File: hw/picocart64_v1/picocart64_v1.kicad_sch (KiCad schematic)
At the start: 16 parts, among them J1 USB_C_Receptacle_USB2.0, J2 Conn_01x05, J3 Conn_02x06_Odd_Even, J4 Micro_SD_Card_Det, Q1 BSS84, SW1 BootButton, U3 RP2040_Stamp, U4 N64-Cartridge

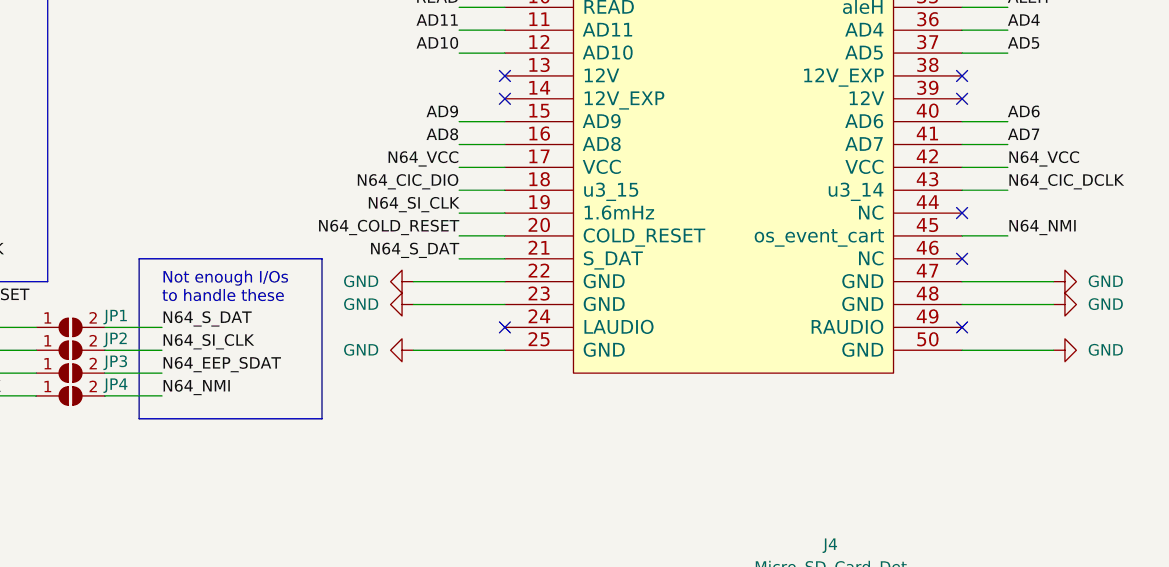
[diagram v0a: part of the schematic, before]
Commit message: hw: PicoCart64 V1.1
- KiCad project files
- Gerbers
- PDF
- Changelog since V1.0 + errata
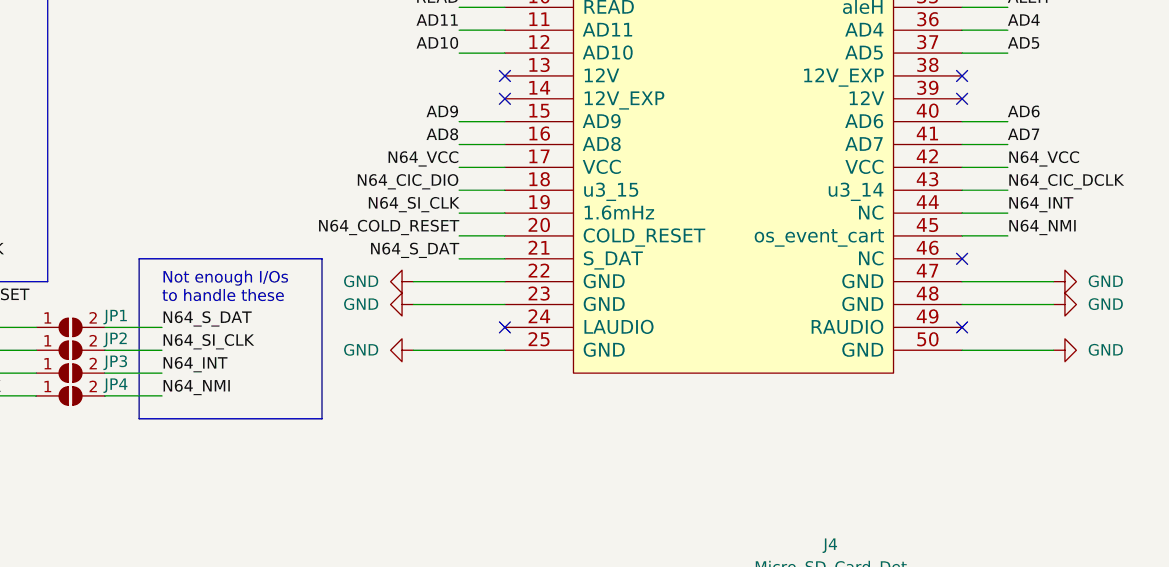
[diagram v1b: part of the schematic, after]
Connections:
- net N64_EEP_SDAT is gone; now on net N64_INT: JP3.2 (B)
- net N64_INT: now reaches U4.44 (NC)
- no-connect marks 12 -> 11
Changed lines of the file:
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@@
   (title_block
     (title "PicoCart64")
-    (date "2022-06-22")
-    (rev "V1.0")
+    (date "2022-07-02")
+    (rev "V1.1")
     (company "Konrad Beckmann")
   )
@@
   (no_connect (at 205.74 55.88))
   (no_connect (at 256.54 76.2))
-  (no_connect (at 256.54 71.12))
   (wire (pts (xy 256.54 86.36) (xy 266.7 86.36))
     (stroke (width 0) (type default) (color 0 0 0 0))
@@
   )
   (wire (pts (xy 115.57 129.54) (xy 120.65 129.54))
+    (stroke (width 0) (type default) (color 0 0 0 0))
+  )
+  (wire (pts (xy 256.54 71.12) (xy 261.62 71.12))
     (stroke (width 0) (type default) (color 0 0 0 0))
   )
@@
     (effects (font (size 1.27 1.27)) (justify right bottom))
   )
+  (label "N64_INT" (at 261.62 71.12 0)
+    (effects (font (size 1.27 1.27)) (justify left bottom))
+  )
   (label "PMOD_1_SS" (at 213.36 124.46 180)
     (effects (font (size 1.27 1.27)) (justify right bottom))
@@
     (effects (font (size 1.27 1.27)) (justify left bottom))
   )
-  (label "N64_EEP_SDAT" (at 167.64 88.9 0)
-    (effects (font (size 1.27 1.27)) (justify left bottom))
-  )
+  (label "N64_INT" (at 167.64 88.9 0)
+    (effects (font (size 1.27 1.27)) (justify left bottom))
+  )
